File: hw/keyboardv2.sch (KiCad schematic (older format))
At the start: 17 parts, among them U1 TINYMEGA

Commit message: Add decaps, make schematic fit for PCB, start PCB
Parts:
- added C1: 100n, ~, symbol C
- added C2, C3, C4, C5: 10u, ~, symbol CP1
- gave numbers to parts that had none: 15
- renumbered BLAU to ROTL1
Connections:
- net GND: now also ROTL1.1 (P1), C1.2, C2.2, C3.2, C4.2, C5.2; no longer ROTL1.3 (P3)
- net LCD_RW: now also U1.29 (F1)
- net VDD: now also ROTL1.3 (P3), C1.1, C2.1, C3.1, C4.1, C5.1; no longer ROTL1.1 (P1)
- no-connect marks 4 -> 11

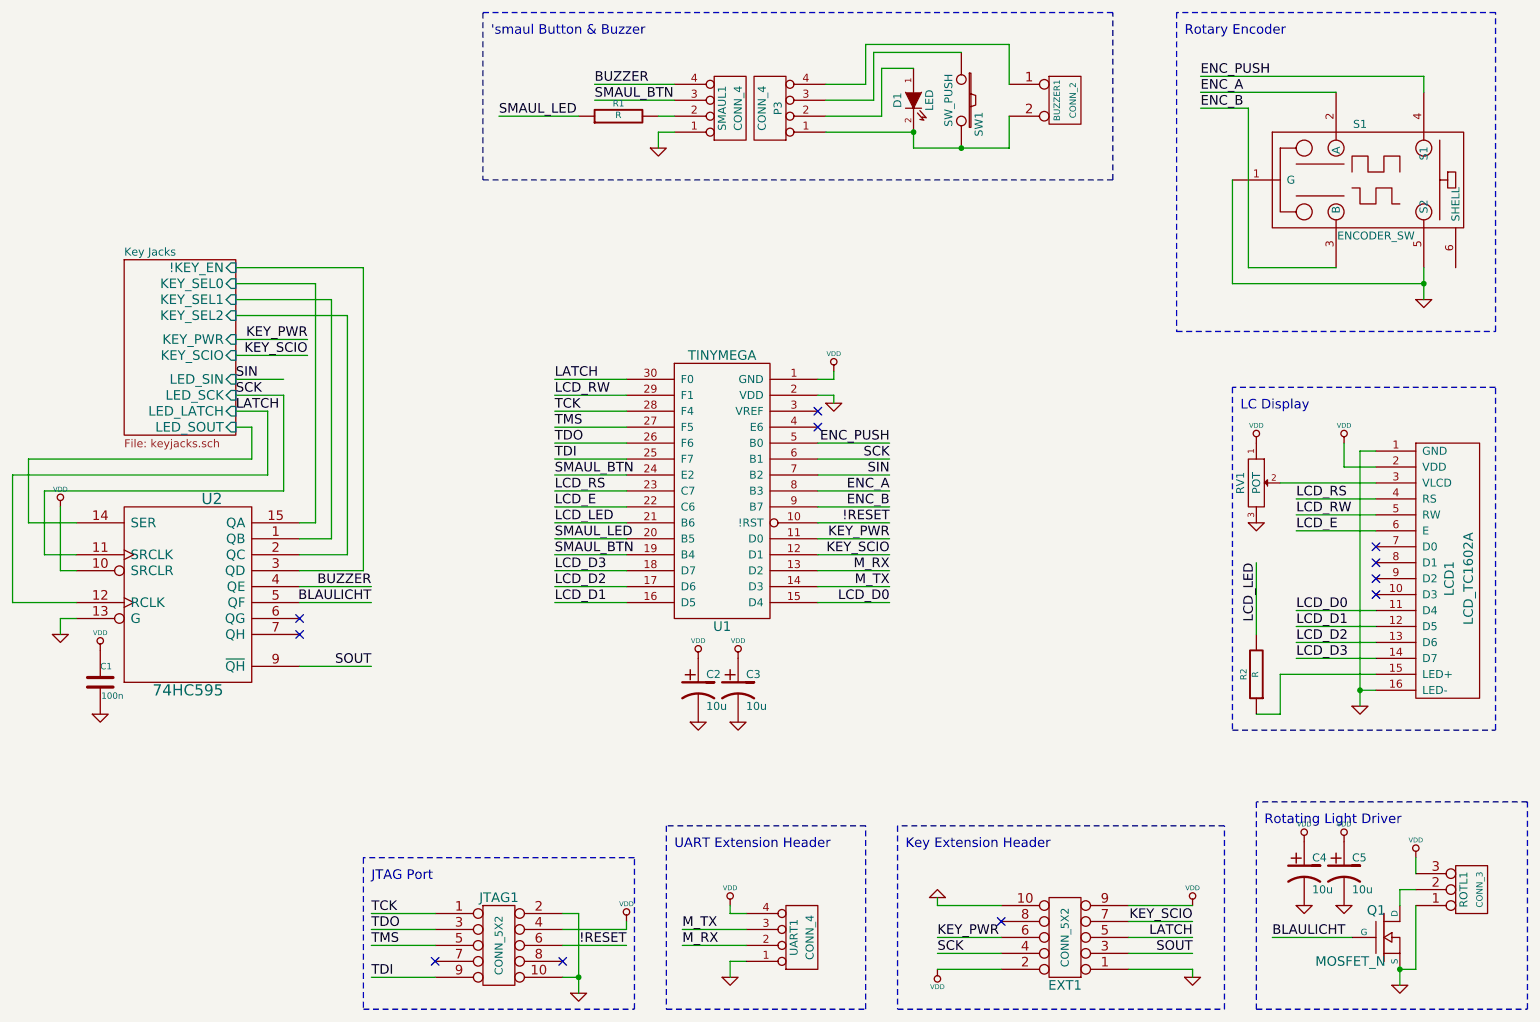
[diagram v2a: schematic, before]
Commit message: Routed all signals, only VDD/GND remaining
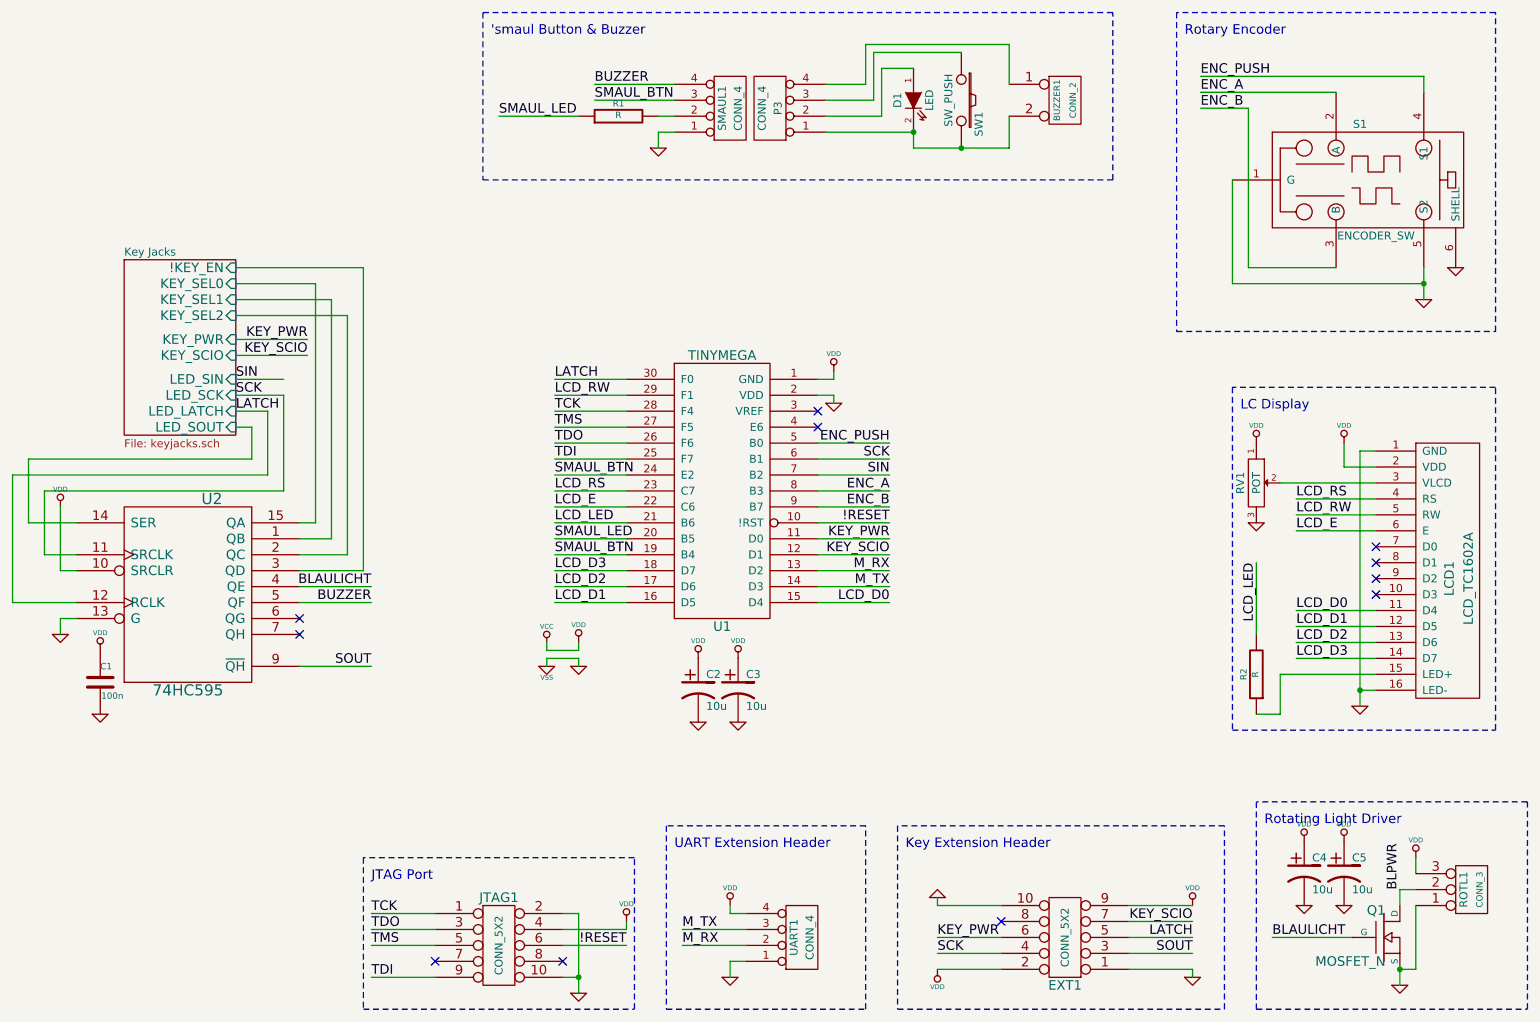
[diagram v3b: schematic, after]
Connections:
- net VDD is gone; now on net VCC: C1.1, C2.1, C3.1, C4.1, C5.1, EXT1.2, EXT1.9, JTAG1.4, LCD1.2 (VDD), ROTL1.3 (P3), RV1.1, U1.1 (GND), U2.10 (SRCLR), UART1.4 (P4)
- net BLAULICHT: now also U2.4 (QE); no longer U2.5 (QF)
- net BUZZER: now also U2.5 (QF); no longer U2.4 (QE)
- net GND: now also S1.6 (SHELL)
- net BLPWR: now reaches Q1.D, ROTL1.2 (PM)
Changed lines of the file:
@@
 Sheet 1 2
 Title ""
-Date "15 nov 2013"
+Date "16 nov 2013"
 Rev ""
 Comp ""
@@
 $EndComp
 $Comp
-L GND #PWR30
+L GND #PWR01
 U 1 1 52643422
 P 10450 2550
-F 0 "#PWR30" H 10450 2550 30  0001 C CNN
+F 0 "#PWR01" H 10450 2550 30  0001 C CNN
 F 1 "GND" H 10450 2480 30  0001 C CNN
 F 2 "" H 10450 2550 60  0000 C CNN
@@
 $EndComp
 $Comp
-L GND #PWR15
+L GND #PWR02
 U 1 1 52645405
 P 6750 3200
-F 0 "#PWR15" H 6750 3200 30  0001 C CNN
+F 0 "#PWR02" H 6750 3200 30  0001 C CNN
 F 1 "GND" H 6750 3130 30  0001 C CNN
 F 2 "" H 6750 3200 60  0000 C CNN
@@
 $EndComp
 $Comp
-L VDD #PWR14
+L VDD #PWR03
 U 1 1 5264541E
 P 6750 3000
-F 0 "#PWR14" H 6750 3100 30  0001 C CNN
+F 0 "#PWR03" H 6750 3100 30  0001 C CNN
 F 1 "VDD" H 6750 3110 30  0000 C CNN
 F 2 "" H 6750 3000 60  0000 C CNN
@@
 $EndComp
 $Comp
-L GND #PWR2
+L GND #PWR04
 U 1 1 527525EF
 P 1900 4650
-F 0 "#PWR2" H 1900 4650 30  0001 C CNN
+F 0 "#PWR04" H 1900 4650 30  0001 C CNN
 F 1 "GND" H 1900 4580 30  0001 C CNN
 F 2 "" H 1900 4650 60  0000 C CNN
@@
 $EndComp
 $Comp
-L VDD #PWR1
+L VDD #PWR05
 U 1 1 527525F5
 P 1900 3850
-F 0 "#PWR1" H 1900 3950 30  0001 C CNN
+F 0 "#PWR05" H 1900 3950 30  0001 C CNN
 F 1 "VDD" H 1900 3960 30  0000 C CNN
 F 2 "" H 1900 3850 60  0000 C CNN
@@
 NoConn ~ 10150 4400
 $Comp
-L VDD #PWR24
+L VDD #PWR06
 U 1 1 52752615
 P 9950 3450
-F 0 "#PWR24" H 9950 3550 30  0001 C CNN
+F 0 "#PWR06" H 9950 3550 30  0001 C CNN
 F 1 "VDD" H 9950 3560 30  0000 C CNN
 F 2 "" H 9950 3450 60  0000 C CNN
@@
 $EndComp
 $Comp
-L VDD #PWR20
+L VDD #PWR07
 U 1 1 5275261B
 P 9400 3450
-F 0 "#PWR20" H 9400 3550 30  0001 C CNN
+F 0 "#PWR07" H 9400 3550 30  0001 C CNN
 F 1 "VDD" H 9400 3560 30  0000 C CNN
 F 2 "" H 9400 3450 60  0000 C CNN
@@
 $EndComp
 $Comp
-L GND #PWR21
+L GND #PWR08
 U 1 1 52752622
 P 9400 3950
-F 0 "#PWR21" H 9400 3950 30  0001 C CNN
+F 0 "#PWR08" H 9400 3950 30  0001 C CNN
 F 1 "GND" H 9400 3880 30  0001 C CNN
 F 2 "" H 9400 3950 60  0000 C CNN
@@
 $EndComp
 $Comp
-L GND #PWR27
+L GND #PWR09
 U 1 1 52752628
 P 10050 5100
-F 0 "#PWR27" H 10050 5100 30  0001 C CNN
+F 0 "#PWR09" H 10050 5100 30  0001 C CNN
 F 1 "GND" H 10050 5030 30  0001 C CNN
 F 2 "" H 10050 5100 60  0000 C CNN
@@
 $EndComp
 $Comp
-L GND #PWR28
+L GND #PWR010
 U 1 1 52752649
 P 10300 6850
-F 0 "#PWR28" H 10300 6850 30  0001 C CNN
+F 0 "#PWR010" H 10300 6850 30  0001 C CNN
 F 1 "GND" H 10300 6780 30  0001 C CNN
 F 2 "" H 10300 6850 60  0000 C CNN
@@
 $EndComp
 $Comp
-L VDD #PWR29
+L VDD #PWR011
 U 1 1 52752650
 P 10400 6050
-F 0 "#PWR29" H 10400 6150 30  0001 C CNN
+F 0 "#PWR011" H 10400 6150 30  0001 C CNN
 F 1 "VDD" H 10400 6160 30  0000 C CNN
 F 2 "" H 10400 6050 60  0000 C CNN
@@
 $EndComp
 $Comp
-L GND #PWR7
+L GND #PWR012
 U 1 1 527550FD
 P 5650 1600
-F 0 "#PWR7" H 5650 1600 30  0001 C CNN
+F 0 "#PWR012" H 5650 1600 30  0001 C CNN
 F 1 "GND" H 5650 1530 30  0001 C CNN
 F 2 "" H 5650 1600 60  0000 C CNN
@@
 Wire Wire Line
 	3400 4450 3850 4450
+Text Label 3850 4450 2    60   ~ 0
+BUZZER
 Text Label 3850 4350 2    60   ~ 0
-BUZZER
-Text Label 3850 4450 2    60   ~ 0
 BLAULICHT
 Wire Wire Line
@@
 	8600 6750 9000 6750
 $Comp
-L GND #PWR19
+L GND #PWR013
 U 1 1 5275C1D6
 P 9000 6800
-F 0 "#PWR19" H 9000 6800 30  0001 C CNN
+F 0 "#PWR013" H 9000 6800 30  0001 C CNN
 F 1 "GND" H 9000 6730 30  0001 C CNN
 F 2 "" H 9000 6800 60  0000 C CNN
@@
 $EndComp
 $Comp
-L GND #PWR16
+L GND #PWR014
 U 1 1 5275C1DC
 P 7400 6300
-F 0 "#PWR16" H 7400 6300 30  0001 C CNN
+F 0 "#PWR014" H 7400 6300 30  0001 C CNN
 F 1 "GND" H 7400 6230 30  0001 C CNN
 F 2 "" H 7400 6300 60  0000 C CNN
@@
 $EndComp
 $Comp
-L VDD #PWR18
+L VDD #PWR015
 U 1 1 5275C23C
 P 9000 6350
-F 0 "#PWR18" H 9000 6450 30  0001 C CNN
+F 0 "#PWR015" H 9000 6450 30  0001 C CNN
 F 1 "VDD" H 9000 6460 30  0000 C CNN
 F 2 "" H 9000 6350 60  0000 C CNN
@@
 $EndComp
 $Comp
-L VDD #PWR17
+L VDD #PWR016
 U 1 1 5275C2BA
 P 7400 6750
-F 0 "#PWR17" H 7400 6850 30  0001 C CNN
+F 0 "#PWR016" H 7400 6850 30  0001 C CNN
 F 1 "VDD" H 7400 6860 30  0000 C CNN
 F 2 "" H 7400 6750 60  0000 C CNN
@@
 $EndComp
 $Comp
-L GND #PWR11
+L GND #PWR017
 U 1 1 5275C8DD
 P 6100 6800
-F 0 "#PWR11" H 6100 6800 30  0001 C CNN
+F 0 "#PWR017" H 6100 6800 30  0001 C CNN
 F 1 "GND" H 6100 6730 30  0001 C CNN
 F 2 "" H 6100 6800 60  0000 C CNN
@@
 $EndComp
 $Comp
-L VDD #PWR10
+L VDD #PWR018
 U 1 1 5275C8E3
 P 6100 6350
-F 0 "#PWR10" H 6100 6450 30  0001 C CNN
+F 0 "#PWR018" H 6100 6450 30  0001 C CNN
 F 1 "VDD" H 6100 6460 30  0000 C CNN
 F 2 "" H 6100 6350 60  0000 C CNN
@@
 	5050 6600 5450 6600
 $Comp
-L GND #PWR5
+L GND #PWR019
 U 1 1 5275D042
 P 5150 6900
-F 0 "#PWR5" H 5150 6900 30  0001 C CNN
+F 0 "#PWR019" H 5150 6900 30  0001 C CNN
 F 1 "GND" H 5150 6830 30  0001 C CNN
 F 2 "" H 5150 6900 60  0000 C CNN
@@
 $EndComp
 $Comp
-L VDD #PWR6
+L VDD #PWR020
 U 1 1 5275D048
 P 5450 6450
-F 0 "#PWR6" H 5450 6550 30  0001 C CNN
+F 0 "#PWR020" H 5450 6550 30  0001 C CNN
 F 1 "VDD" H 5450 6560 30  0000 C CNN
 F 2 "" H 5450 6450 60  0000 C CNN
@@
 $EndComp
 $Comp
-L GND #PWR9
+L GND #PWR021
 U 1 1 5283EAA6
 P 5900 5200
-F 0 "#PWR9" H 5900 5200 30  0001 C CNN
+F 0 "#PWR021" H 5900 5200 30  0001 C CNN
 F 1 "GND" H 5900 5130 30  0001 C CNN
 F 2 "" H 5900 5200 60  0000 C CNN
@@
 $EndComp
 $Comp
-L VDD #PWR8
+L VDD #PWR022
 U 1 1 5283EAAC
 P 5900 4800
-F 0 "#PWR8" H 5900 4900 30  0001 C CNN
+F 0 "#PWR022" H 5900 4900 30  0001 C CNN
 F 1 "VDD" H 5900 4910 30  0000 C CNN
 F 2 "" H 5900 4800 60  0000 C CNN
@@
 $EndComp
 $Comp
-L GND #PWR13
+L GND #PWR023
 U 1 1 5283EB53
 P 6150 5200
-F 0 "#PWR13" H 6150 5200 30  0001 C CNN
+F 0 "#PWR023" H 6150 5200 30  0001 C CNN
 F 1 "GND" H 6150 5130 30  0001 C CNN
 F 2 "" H 6150 5200 60  0000 C CNN
@@
 $EndComp
 $Comp
-L VDD #PWR12
+L VDD #PWR024
 U 1 1 5283EB59
 P 6150 4800
-F 0 "#PWR12" H 6150 4900 30  0001 C CNN
+F 0 "#PWR024" H 6150 4900 30  0001 C CNN
 F 1 "VDD" H 6150 4910 30  0000 C CNN
 F 2 "" H 6150 4800 60  0000 C CNN
@@
 $EndComp
 $Comp
-L GND #PWR23
+L GND #PWR025
 U 1 1 5283EB83
 P 9700 6350
-F 0 "#PWR23" H 9700 6350 30  0001 C CNN
+F 0 "#PWR025" H 9700 6350 30  0001 C CNN
 F 1 "GND" H 9700 6280 30  0001 C CNN
 F 2 "" H 9700 6350 60  0000 C CNN
@@
 $EndComp
 $Comp
-L VDD #PWR22
+L VDD #PWR026
 U 1 1 5283EB89
 P 9700 5950
-F 0 "#PWR22" H 9700 6050 30  0001 C CNN
+F 0 "#PWR026" H 9700 6050 30  0001 C CNN
 F 1 "VDD" H 9700 6060 30  0000 C CNN
 F 2 "" H 9700 5950 60  0000 C CNN
@@
 $EndComp
 $Comp
-L GND #PWR26
+L GND #PWR027
 U 1 1 5283EB95
 P 9950 6350
-F 0 "#PWR26" H 9950 6350 30  0001 C CNN
+F 0 "#PWR027" H 9950 6350 30  0001 C CNN
 F 1 "GND" H 9950 6280 30  0001 C CNN
 F 2 "" H 9950 6350 60  0000 C CNN
@@
 $EndComp
 $Comp
-L VDD #PWR25
+L VDD #PWR028
 U 1 1 5283EB9B
 P 9950 5950
-F 0 "#PWR25" H 9950 6050 30  0001 C CNN
+F 0 "#PWR028" H 9950 6050 30  0001 C CNN
 F 1 "VDD" H 9950 6060 30  0000 C CNN
 F 2 "" H 9950 5950 60  0000 C CNN
@@
 $EndComp
 $Comp
-L VDD #PWR3
+L VDD #PWR029
 U 1 1 5283F326
 P 2150 4750
-F 0 "#PWR3" H 2150 4850 30  0001 C CNN
+F 0 "#PWR029" H 2150 4850 30  0001 C CNN
 F 1 "VDD" H 2150 4860 30  0000 C CNN
 F 2 "" H 2150 4750 60  0000 C CNN
@@
 $EndComp
 $Comp
-L GND #PWR4
+L GND #PWR030
 U 1 1 5283F32C
 P 2150 5150
-F 0 "#PWR4" H 2150 5150 30  0001 C CNN
+F 0 "#PWR030" H 2150 5150 30  0001 C CNN
 F 1 "GND" H 2150 5080 30  0001 C CNN
 F 2 "" H 2150 5150 60  0000 C CNN
@@
 	1    0    0    -1
 $EndComp
+Text Label 10300 6250 1    60   ~ 0
+BLPWR
+$Comp
+L GND #PWR031
+U 1 1 528747E4
+P 10650 2350
+F 0 "#PWR031" H 10650 2350 30  0001 C CNN
+F 1 "GND" H 10650 2280 30  0001 C CNN
+F 2 "" H 10650 2350 60  0000 C CNN
+F 3 "" H 10650 2350 60  0000 C CNN
+	1    10650 2350
+	1    0    0    -1
+$EndComp
+$Comp
+L VSS #PWR032
+U 1 1 52875000
+P 4950 4850
+F 0 "#PWR032" H 4950 4850 30  0001 C CNN
+F 1 "VSS" H 4950 4780 30  0000 C CNN
+F 2 "" H 4950 4850 60  0000 C CNN
+F 3 "" H 4950 4850 60  0000 C CNN
+	1    4950 4850
+	1    0    0    -1
+$EndComp
+$Comp
+L GND #PWR033
+U 1 1 52875006
+P 5150 4850
+F 0 "#PWR033" H 5150 4850 30  0001 C CNN
+F 1 "GND" H 5150 4780 30  0001 C CNN
+F 2 "" H 5150 4850 60  0000 C CNN
+F 3 "" H 5150 4850 60  0000 C CNN
+	1    5150 4850
+	1    0    0    -1
+$EndComp
+Wire Wire Line
+	4950 4850 4950 4800
+Wire Wire Line
+	4950 4800 5150 4800
+Wire Wire Line
+	5150 4800 5150 4850
+$Comp
+L VCC #PWR034
+U 1 1 528750B1
+P 4950 4700
+F 0 "#PWR034" H 4950 4800 30  0001 C CNN
+F 1 "VCC" H 4950 4800 30  0000 C CNN
+F 2 "" H 4950 4700 60  0000 C CNN
+F 3 "" H 4950 4700 60  0000 C CNN
+	1    4950 4700
+	1    0    0    -1
+$EndComp
+$Comp
+L VDD #PWR035
+U 1 1 52875172
+P 5150 4700
+F 0 "#PWR035" H 5150 4800 30  0001 C CNN
+F 1 "VDD" H 5150 4810 30  0000 C CNN
+F 2 "" H 5150 4700 60  0000 C CNN
+F 3 "" H 5150 4700 60  0000 C CNN
+	1    5150 4700
+	1    0    0    -1
+$EndComp
+Wire Wire Line
+	4950 4700 4950 4750
+Wire Wire Line
+	4950 4750 5150 4750
+Wire Wire Line
+	5150 4750 5150 4700
 $EndSCHEMATC

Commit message: All connections routed! \o/
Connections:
- net GND: now also RV1.1; no longer RV1.3
- net VCC: now also RV1.3; no longer RV1.1
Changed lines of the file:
@@
 F 3 "~" H 9400 3700 60  0000 C CNN
 	1    9400 3700
-	0    1    1    0
+	0    1    -1   0
 $EndComp
 NoConn ~ 10150 4100

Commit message: Yeah, so I had the board reversed -.-   Once more with feeling.
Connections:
- net GND: now also RV1.3; no longer RV1.1
- net VCC: now also RV1.1; no longer RV1.3
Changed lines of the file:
@@
 Sheet 1 2
 Title ""
-Date "16 nov 2013"
+Date "17 nov 2013"
 Rev ""
 Comp ""
@@
 F 3 "~" H 9400 3700 60  0000 C CNN
 	1    9400 3700
-	0    1    -1   0
+	0    1    1    0
 $EndComp
 NoConn ~ 10150 4100
